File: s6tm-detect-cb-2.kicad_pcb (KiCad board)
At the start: 4 copper layers, 175 parts, among them J1 Conn_Coaxial, J2 Conn_01x04_Pin, J3 USB_C_Receptacle_USB2.0_14P, J4 Conn_01x04, J5 Conn_01x04, J6 USB_C_Receptacle_USB2.0_14P, J7 Conn_01x04_Pin, J8 SIM_Card_Shielded, J9 Conn_Coaxial, Q1 AO3400A, Q2 MMBT3904, Q3 MMBT3904, Q4 MMBT3904, SW1 SW_Push, SW2 SW_Push, SW3 SW_Push, SW4 SW_Push, U1 W25Q128JVS, U10 TPS6282x, U11 TPS6282x, U12 TPS259472A, U13 TPD3F303DPV, U14 SIM7080G, U15 SN74LV1T125DBV, U16 SN74LV1T125DBV, U17 SN74LV1T125DBV, U18 SN74LV1T125DBV, U19 SN74LV1T125DBV, U2 SN65HVD230, U3 PCF85263ATL, U4 MS5607, U5 ESP32-S3FH4R2, U6 HTU21, U8 VL53L0CXV0DH1, U9 NextPM, Y1 32k768, Y2 48M

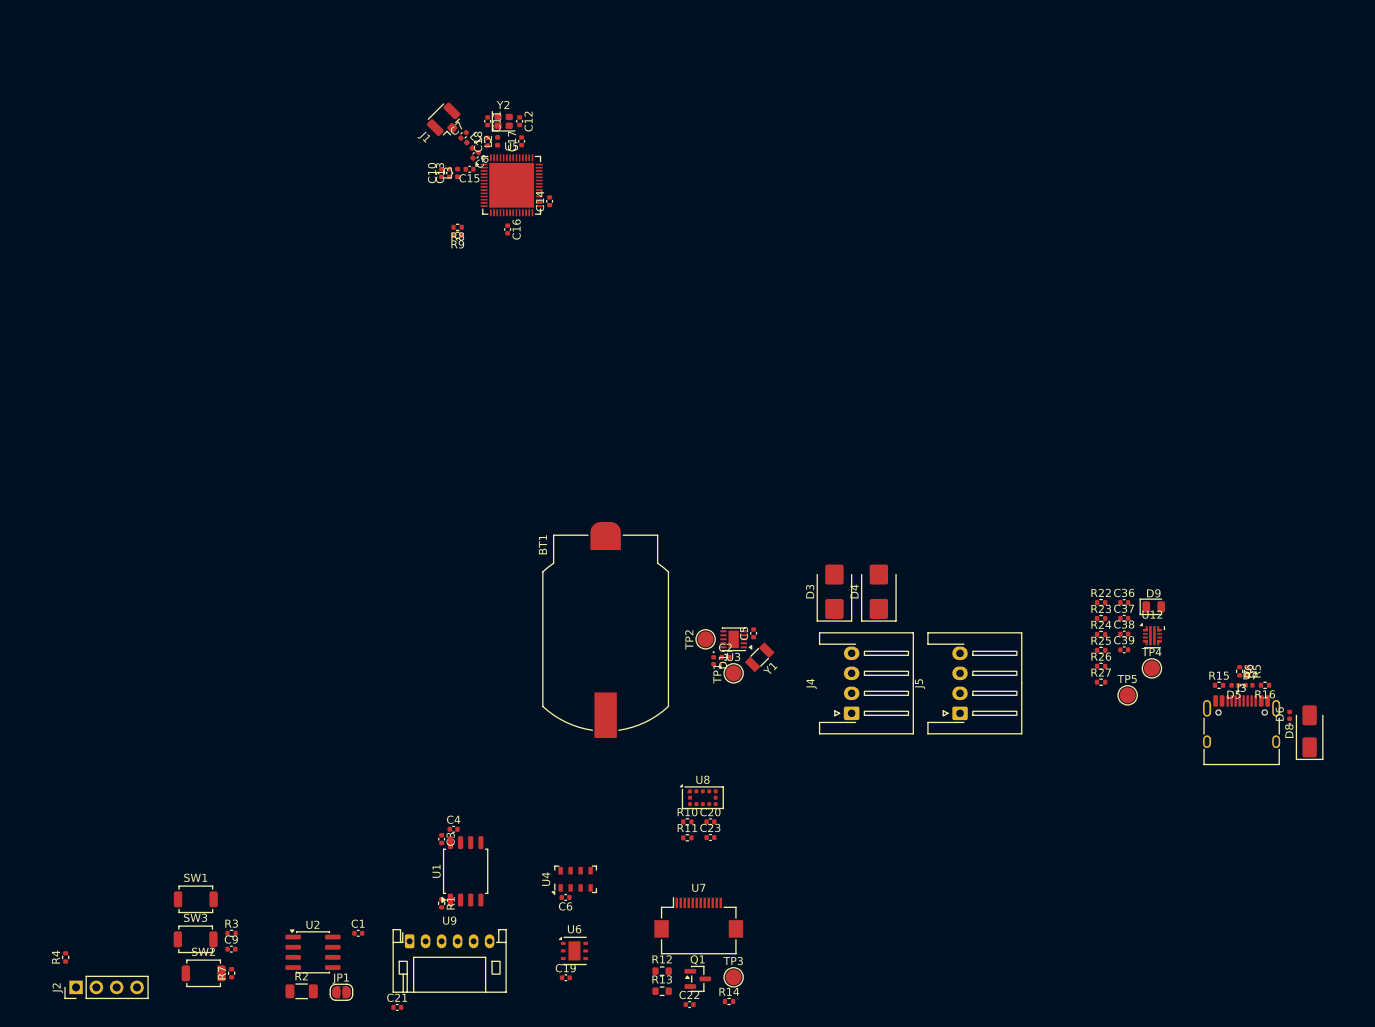
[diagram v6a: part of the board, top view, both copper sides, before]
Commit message: pcb: route can connectors
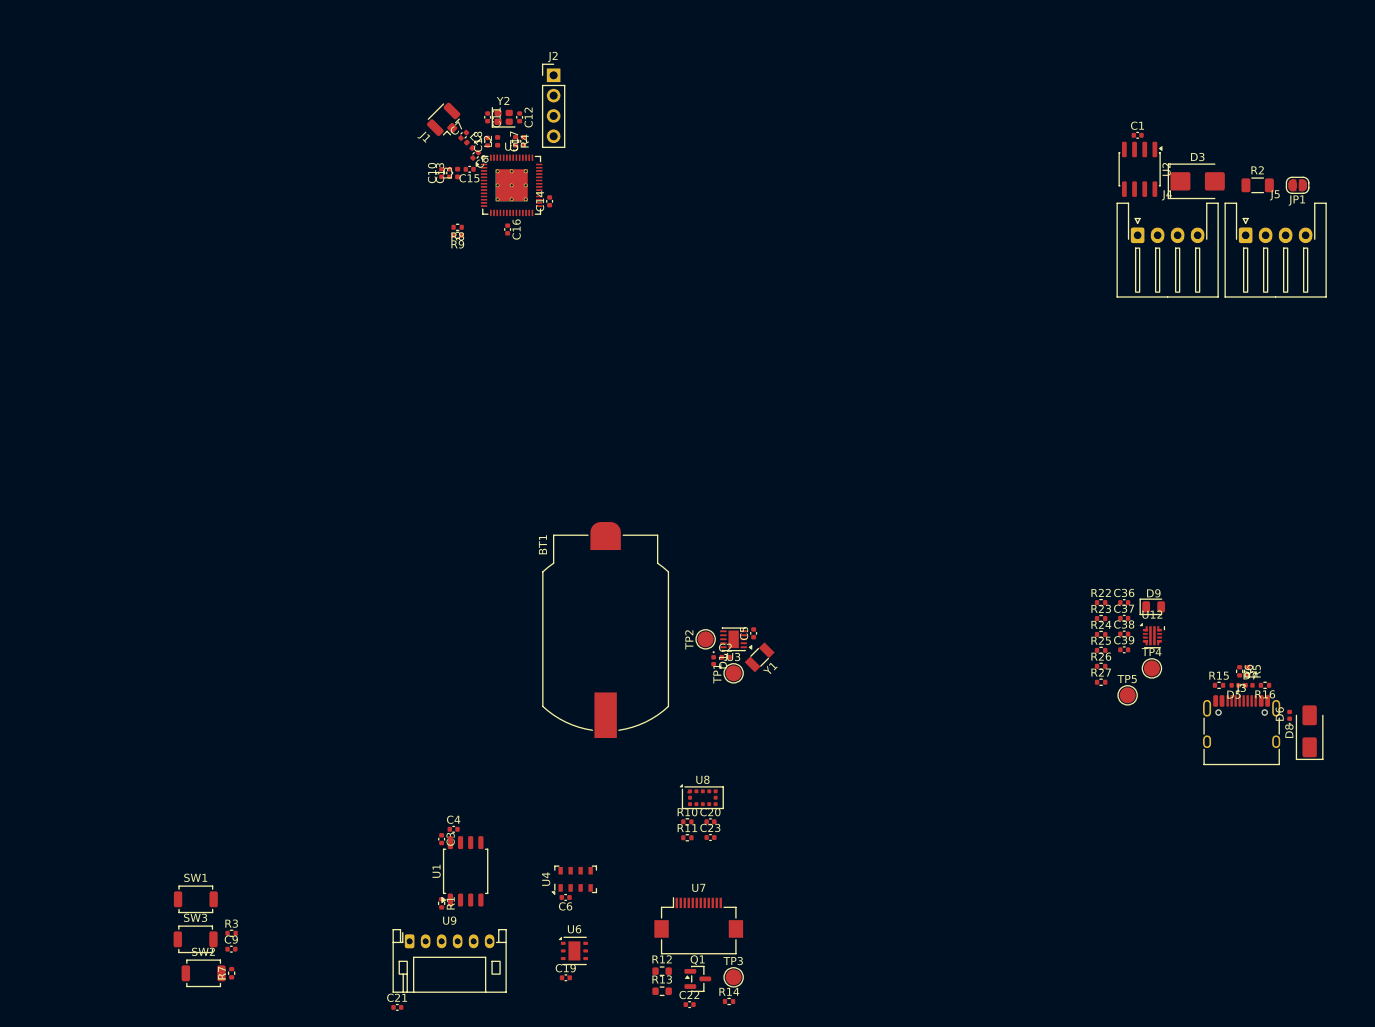
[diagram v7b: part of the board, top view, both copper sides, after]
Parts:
- removed D4: SMBJ6.0CA, Diode_SMD:D_SMB
- U5: footprint Package_DFN_QFN:QFN-56-1EP_7x7mm_P0.4mm_EP5.6x5.6mm -> Package_DFN_QFN:QFN-56-1EP_7x7mm_P0.4mm_EP4x4mm_ThermalVias
- moved JP1 156.4 mm to (242.0, 91.8), turned to 180 degrees
- moved R2 156.3 mm to (237.0, 91.8)
- moved U2 142.3 mm to (222.2, 89.8), turned to -90 degrees
- moved C1 139.4 mm to (222.0, 85.5)
- moved J2 128.7 mm to (149.0, 78.0), turned to 0 degrees
- moved R4 116.5 mm to (144.2, 86.2), turned to -90 degrees
- moved J4 69.6 mm to (222.0, 98.0), turned to 0 degrees
- moved J5 69.6 mm to (235.5, 98.0), turned to 0 degrees
- moved D3 68.5 mm to (229.5, 91.2), turned to 0 degrees
- moved C11 0.50 mm to (140.8, 83.2)
- moved C12 0.50 mm to (144.8, 83.2)
- moved Y2 0.50 mm to (142.8, 83.2)
- moved C17 0.25 mm to (145.2, 86.2)
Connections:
- J4 pad 1: /Power/CANH -> CANH
- J4 pad 2: /Power/CANL -> CANL
- J5 pad 1: /Power/CANH -> CANH
- J5 pad 2: /Power/CANL -> CANL
- JP1 pad 1: /CANL -> CANL
- R2 pad 1: /CANH -> CANH
- U2 pad 6: /CANL -> CANL
- U2 pad 7: /CANH -> CANH

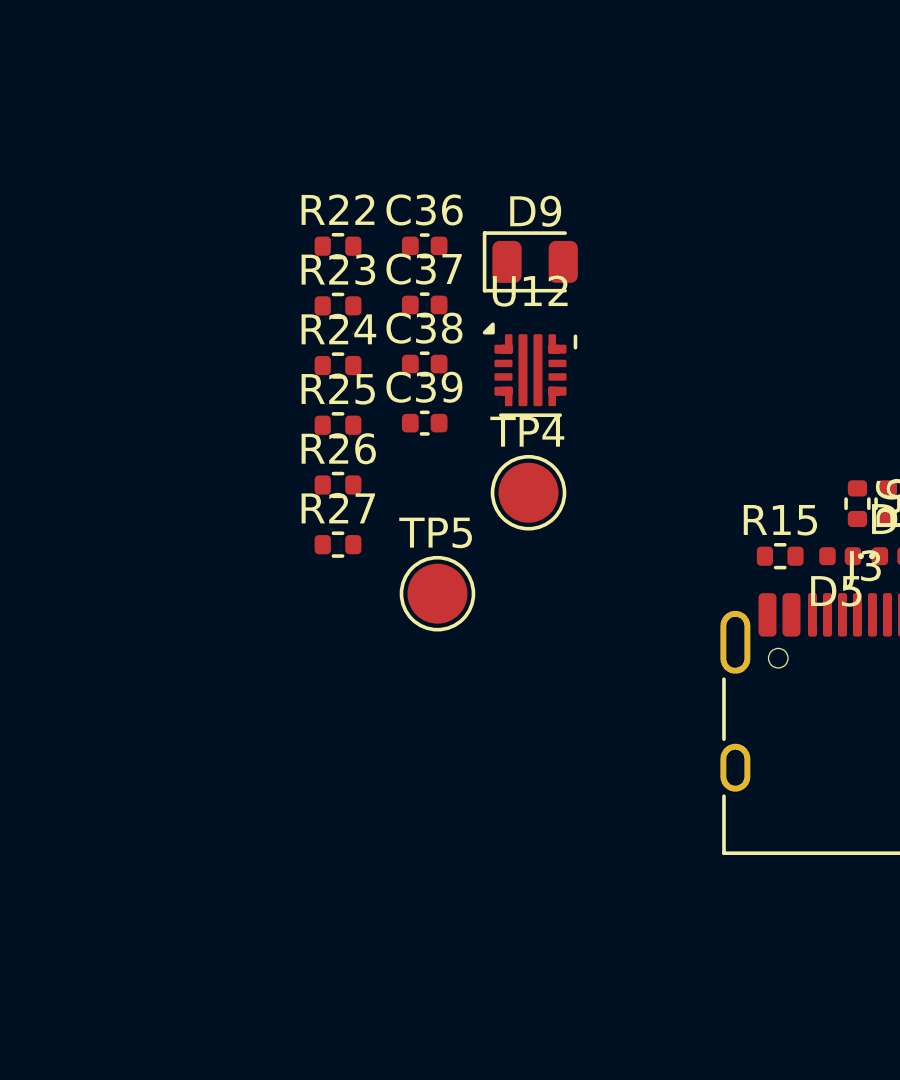
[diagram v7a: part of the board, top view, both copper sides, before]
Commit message: pcb: add +5v efuse layout
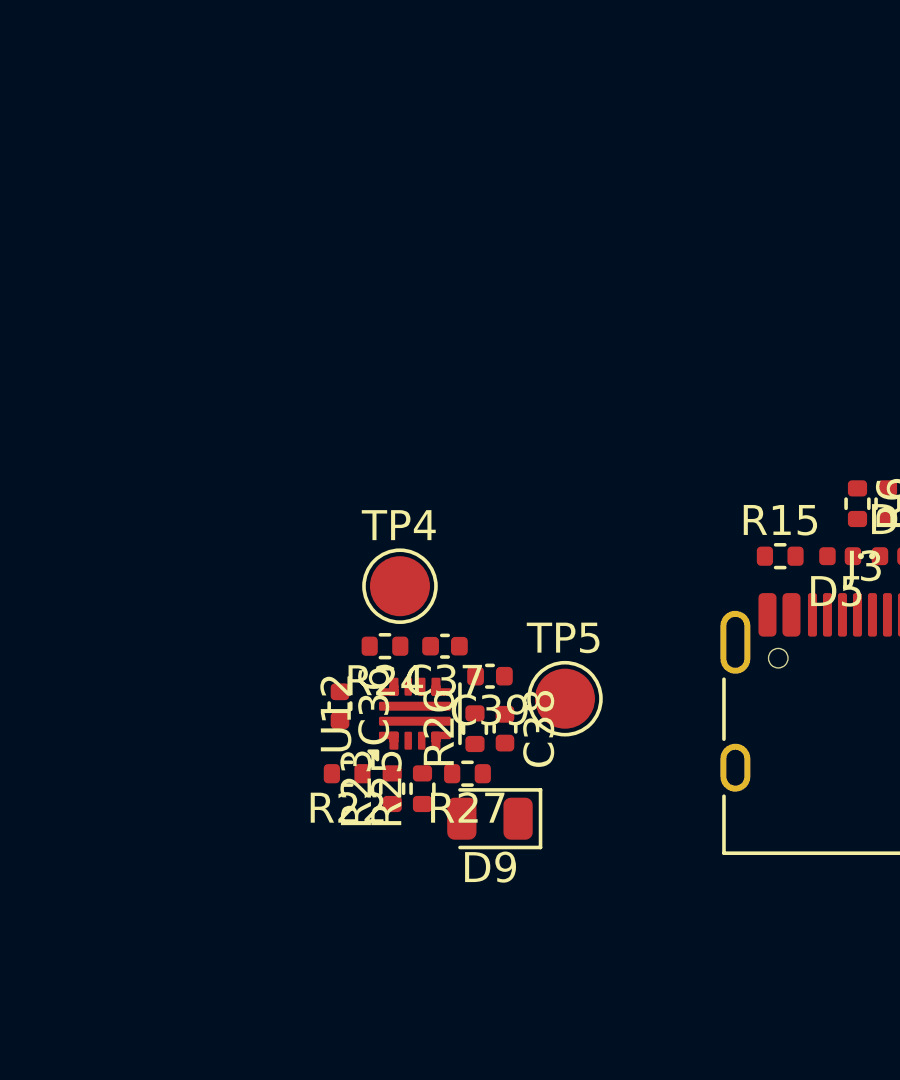
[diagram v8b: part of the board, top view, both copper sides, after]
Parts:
- moved D9 18.6 mm to (222.5, 163.0), turned to 180 degrees
- moved R22 17.6 mm to (217.7, 161.5), turned to 180 degrees
- moved R23 16.2 mm to (219.2, 162.0), turned to 90 degrees
- moved C36 15.6 mm to (217.5, 159.2), turned to -90 degrees
- moved C38 12.4 mm to (223.0, 160.0), turned to -90 degrees
- moved R25 12.4 mm to (220.2, 162.0), turned to 90 degrees
- moved U12 12.1 mm to (220.0, 159.5), turned to 90 degrees
- moved C37 11.4 mm to (221.0, 157.2), turned to 180 degrees
- moved R24 9.49 mm to (219.0, 157.2), turned to 180 degrees
- moved R26 9.32 mm to (222.0, 160.0), turned to 90 degrees
- moved R27 8.77 mm to (221.8, 161.5), turned to 180 degrees
- moved C39 8.71 mm to (222.5, 158.2), turned to 180 degrees
- moved TP5 5.51 mm to (225.0, 159.0)
- moved TP4 5.30 mm to (219.5, 155.2)
